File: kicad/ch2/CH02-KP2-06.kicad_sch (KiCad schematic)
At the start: 5 parts

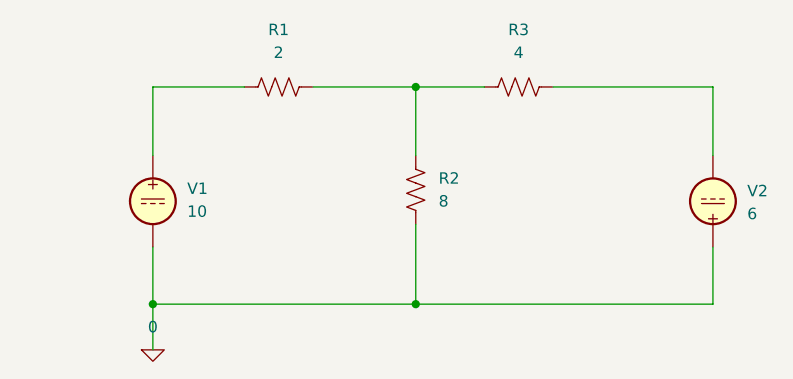
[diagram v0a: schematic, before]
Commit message: fix subsheet sim problem
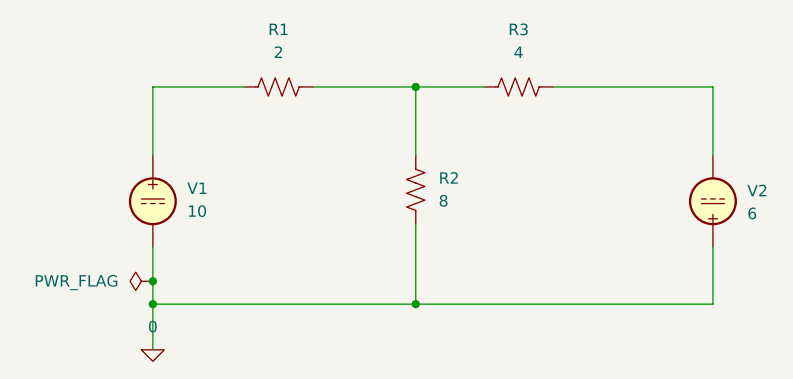
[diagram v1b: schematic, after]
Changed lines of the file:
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@@
 		(color 0 0 0 0)
 	)
+	(junction
+		(at 72.39 74.93)
+		(diameter 0)
+		(color 0 0 0 0)
+	)
 	(wire
 		(pts
@@
 	(wire
 		(pts
+			(xy 72.39 74.93) (xy 72.39 77.47)
+		)
+		(stroke
+			(width 0)
+			(type default)
+		)
+	)
+	(wire
+		(pts
 			(xy 72.39 77.47) (xy 72.39 82.55)
 		)
@@
 	(wire
 		(pts
-			(xy 72.39 71.12) (xy 72.39 77.47)
+			(xy 72.39 71.12) (xy 72.39 74.93)
 		)
 		(stroke
@@
 					(unit 1)
 				)
+			)
+		)
+	)
+	(symbol
+		(lib_id "power:PWR_FLAG")
+		(at 72.39 74.93 90)
+		(unit 1)
+		(exclude_from_sim no)
+		(in_bom yes)
+		(on_board yes)
+		(dnp no)
+		(fields_autoplaced yes)
+		(property "Reference" "#FLG01"
+			(at 70.485 74.93 0)
+			(effects
+				(font
+					(size 1.27 1.27)
+				)
+				(hide yes)
+			)
+		)
+		(property "Value" "PWR_FLAG"
+			(at 68.58 74.9299 90)
+			(effects
+				(font
+					(size 1.27 1.27)
+				)
+				(justify left)
+			)
+		)
+		(property "Footprint" ""
+			(at 72.39 74.93 0)
+			(effects
+				(font
+					(size 1.27 1.27)
+				)
+				(hide yes)
+			)
+		)
+		(property "Datasheet" "~"
+			(at 72.39 74.93 0)
+			(effects
+				(font
+					(size 1.27 1.27)
+				)
+				(hide yes)
+			)
+		)
+		(property "Description" "Special symbol for telling ERC where power comes from"
+			(at 72.39 74.93 0)
+			(effects
+				(font
+					(size 1.27 1.27)
+				)
+				(hide yes)
+			)
+		)
+		(pin "1"
+		)
+		(instances
+			(project ""
+				(path "/fc72c8c5-f743-437f-8eef-093b2f91e0e9/ef48fe50-d047-4f6a-888f-8d940606dc75"
+					(reference "#FLG01")
+					(unit 1)
+				)
